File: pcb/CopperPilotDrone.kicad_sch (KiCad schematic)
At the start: 68 parts, among them IC1 TP4056, J1 USB_C_Receptacle_USB2.0, J2 Conn_01x02_Female, J3 B2B-PH-SM4-TB(LF)(SN), J4 Conn_01x02_Female, J5 Conn_01x02_Female, J6 Conn_01x02_Female, SW1 PCM12SMTR, SW2 TS-1187A, SW3 TS-1187A, T1 SI2302DS-T1, T2 SI2302DS-T1, T3 SI2302DS-T1, T4 SI2302DS-T1, U2 AO3401, U3 AP2112K-3.3TRG1, U8 ESP32-S3-WROOM-1-N8R8, U9 MPU-6050

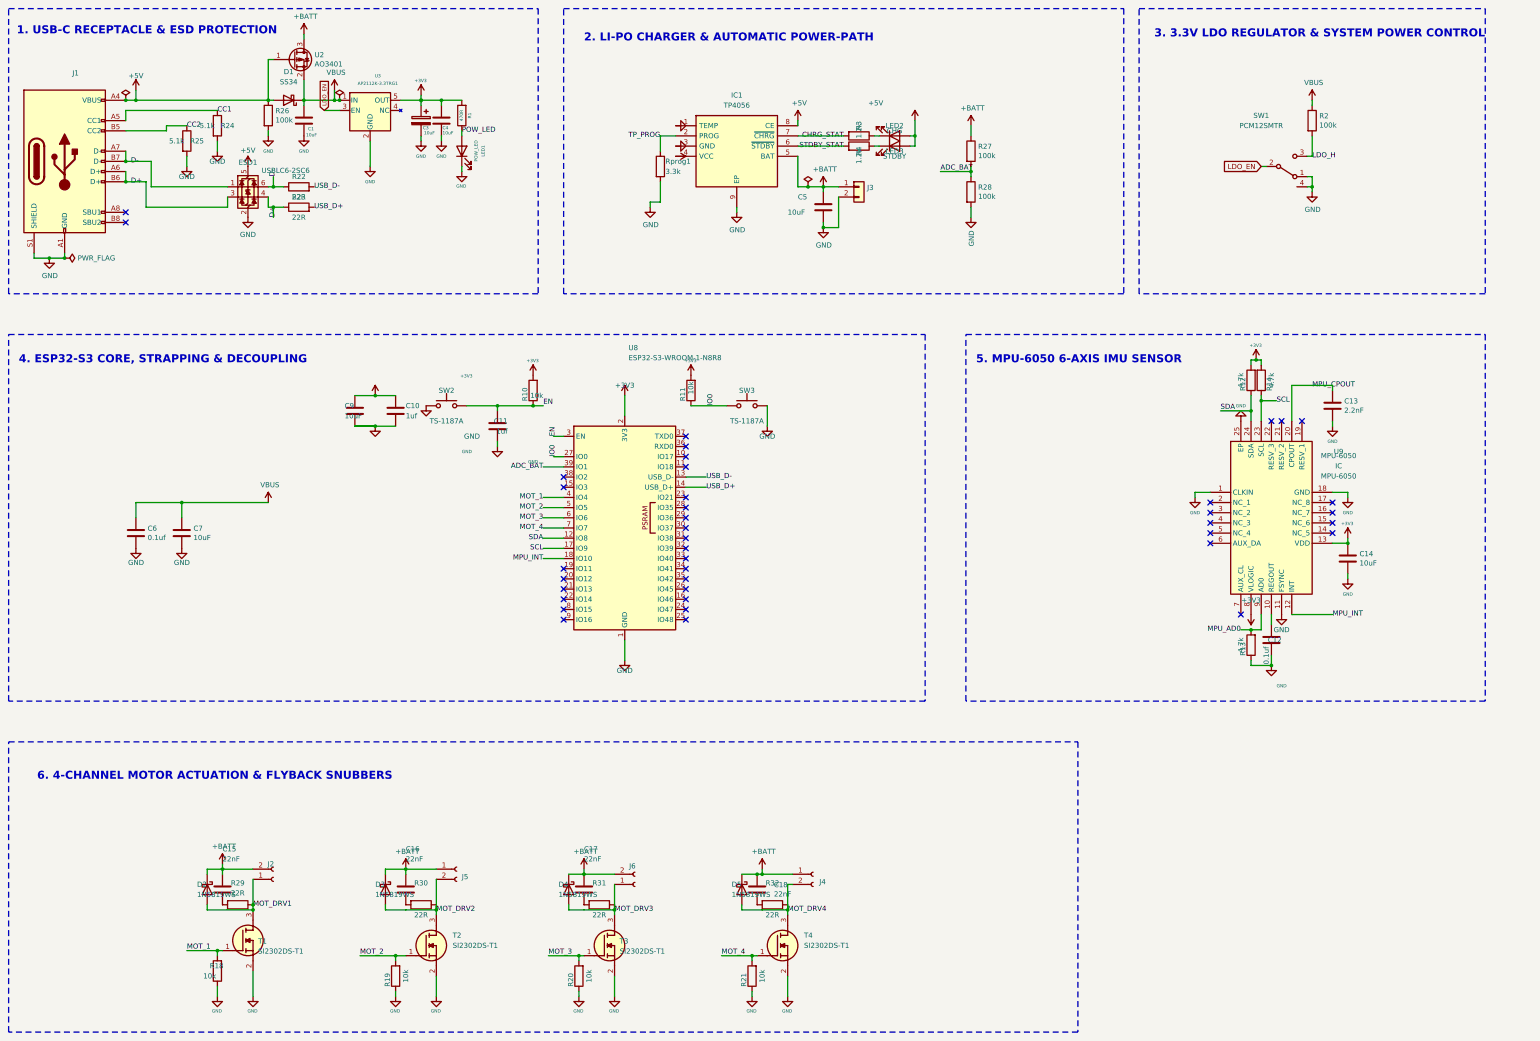
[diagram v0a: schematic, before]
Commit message: feat(pcb,sch,fw): migrate IC1 to MCP73833-AMI/UN and U9 to ICM-42670-P for 100% turnkey PCBA
Replace IC1 (TP4056 ESOP-8) with Microchip MCP73833-AMI/UN (MSOP-10) plus R15 10k THERM bias resistor and replace U9 (MPU-6050 QFN-24) with TDK ICM-42670-P (2.5x3.0mm LGA-14), achieving 0 ERC errors, 0 DRC violations, 0 unconnected items, and 100% turnkey LionCircuits BOM/CPL export with zero DNP.

Co-Authored-By: CopperPilot <noreply@copperpilot.ai>
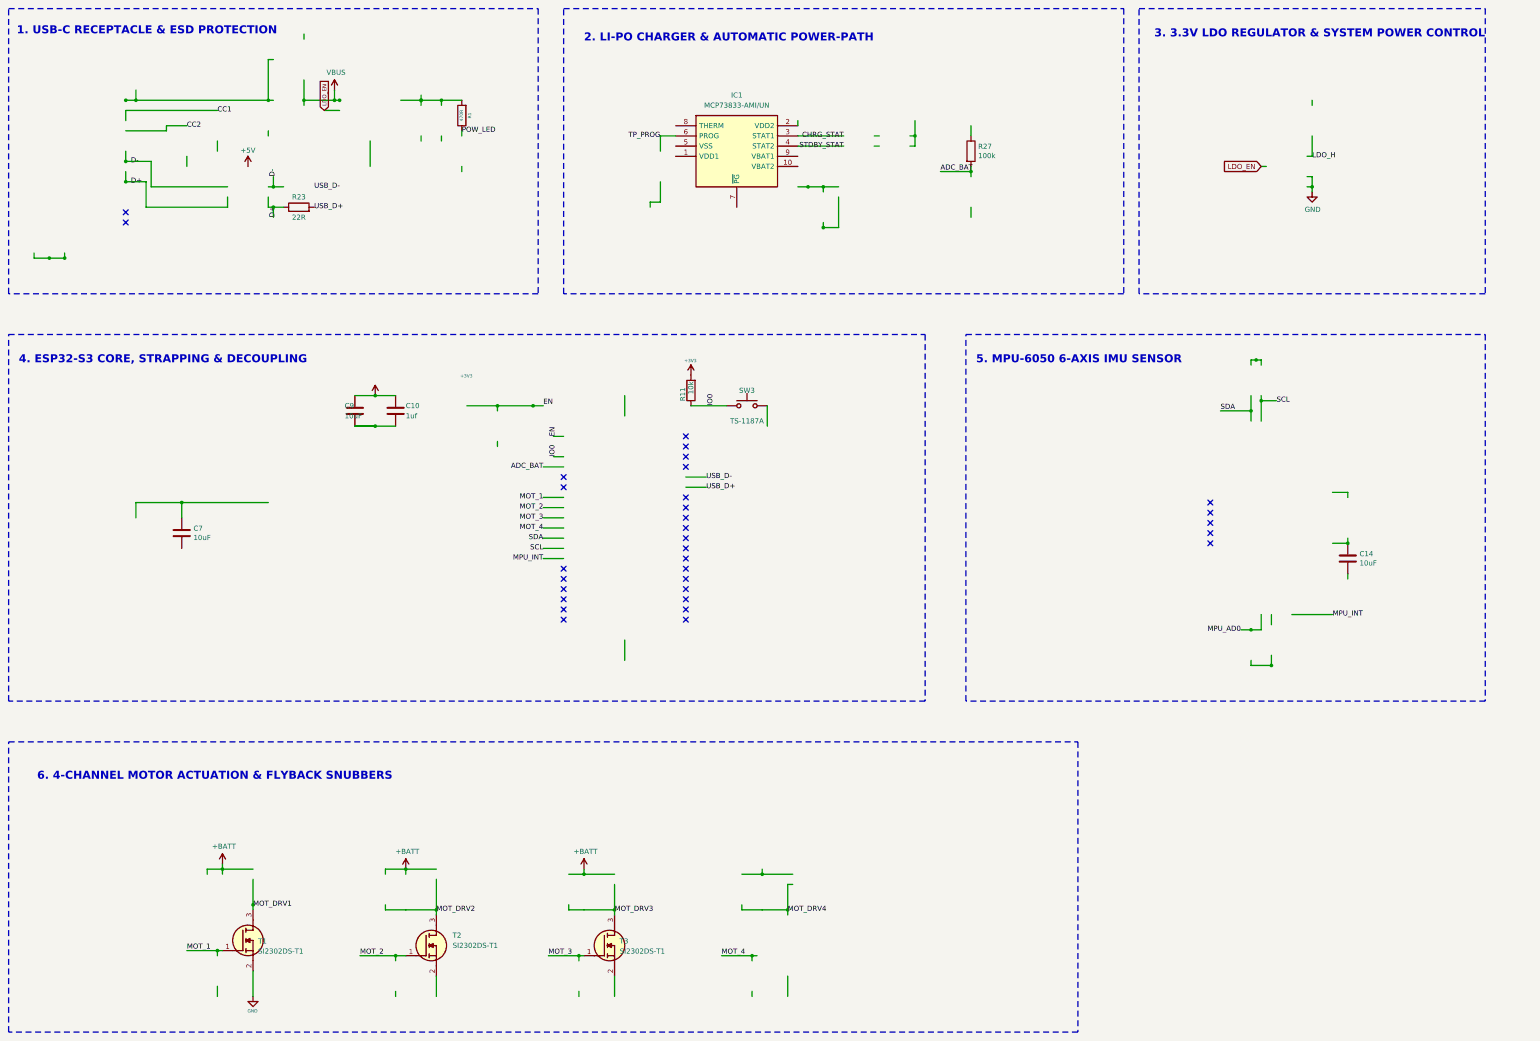
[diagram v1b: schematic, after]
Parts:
- removed C1, C4, C5: 10uF, Capacitor_SMD:C_0603_1608Metric, symbol Device:C
- removed C11: 1uf, Capacitor_SMD:C_0603_1608Metric, symbol Device:C
- removed C12, C6: 0.1uf, Capacitor_SMD:C_0603_1608Metric, symbol Device:C
- removed C13: 2.2nF, Capacitor_SMD:C_0603_1608Metric, symbol Device:C
- removed C15, C16, C17, C18: 22nF, Capacitor_SMD:C_0603_1608Metric, symbol Device:C
- removed C3: 10uF, Capacitor_SMD:C_0603_1608Metric, symbol Device:C_Polarized
- removed D1: SS34, Diode_SMD:D_SMA, symbol Diode:SS34
- removed D2, D3, D4, D5: 1N5819WS, Diode_SMD:D_SOD-323, symbol Diode:1N5819WS
- removed ESD1: USBLC6-2SC6, Package_TO_SOT_SMD:SOT-23-6, symbol Power_Protection:USBLC6-2SC6
- removed J1: USB_C_Receptacle_USB2.0, Connector_USB:USB_C_Receptacle_HRO_TYPE-C-31-M-12, symbol downloader-rescue:USB_C_Receptacle_USB2.0-Connector
- removed J2, J4, J5, J6: Conn_01x02_Female, Connector_JST:JST_GH_SM02B-GHS-TB_1x02-1MP_P1.25mm_Horizontal, symbol Connector:Conn_01x02_Socket
- removed J3: B2B-PH-SM4-TB(LF)(SN), easyeda2kicad:CONN-SMD_B2B-PH-SM4-TB-LF-SN, symbol Connector_Generic:Conn_01x02
- removed LED1: POW_LED, LED_SMD:LED_0603_1608Metric, symbol Device:LED
- removed LED2: CHG, LED_SMD:LED_0603_1608Metric, symbol Device:LED
- removed LED3: STDBY, LED_SMD:LED_0603_1608Metric, symbol Device:LED
- removed R10, R18, R19, R20, R21: 10k, Resistor_SMD:R_0603_1608Metric, symbol Device:R
- removed R12, R13, R14: 4.7k, Resistor_SMD:R_0603_1608Metric, symbol Device:R
- removed R2, R26, R28: 100k, Resistor_SMD:R_0603_1608Metric, symbol Device:R
- removed R22, R29, R30, R31, R32: 22R, Resistor_SMD:R_0603_1608Metric, symbol Device:R
- removed R24, R25: 5.1k, Resistor_SMD:R_0603_1608Metric, symbol Device:R
- removed R3, R4: 1.2k, Resistor_SMD:R_0603_1608Metric, symbol Device:R
- removed Rprog1: 3.3k, Resistor_SMD:R_0603_1608Metric, symbol Device:R
- removed SW1: PCM12SMTR, ESP32_TouchDown_lib:slide switch spdt, symbol ESP32_TouchDown_lib:slide switch spdt
- removed SW2: TS-1187A, Button_Switch_SMD:SW_Push_1P1T_XKB_TS-1187A, symbol Switch:SW_Push
- removed T4: SI2302DS-T1, SI2302DS-T1:SOT95P237X112-3N, symbol SI2302DS-T1:SI2302DS-T1
- removed U2: AO3401, Package_TO_SOT_SMD:SOT-23, symbol Transistor_FET:AO3401A
- removed U3: AP2112K-3.3TRG1, Package_TO_SOT_SMD:SOT-23-5, symbol Regulator_Linear:MIC5219-3.3YM5
- removed U8: ESP32-S3-WROOM-1-N8R8, RF_Module:ESP32-S3-WROOM-1, symbol RF_Module:ESP32-S3-WROOM-1
- removed U9: MPU-6050, MPU6050:MPU6050, symbol MPU-6050:MPU-6050
- IC1: value TP4056 -> MCP73833-AMI/UN; footprint tp4056:SOIC127P600X175-9N -> Package_SO:MSOP-10_3x3mm_P0.5mm; symbol TP4056-42-ESOP8:TP4056-42-ESOP8 -> TP4056-42-ESOP8:MCP73833-AMI-UN; LCSC C16581 -> C47182; Manufacturer_Name Nanjing Extension Microelectronics -> Microchip; Manufacturer_Part_Number TP4056-42-ESOP8 -> MCP73833-AMI/UN
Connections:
- net +3V3: no longer C14.1, R1.2
- net +5V: no longer IC1.4 (VCC), IC1.8 (CE)
- net +BATT: no longer IC1.5 (BAT), R27.1
- net CHRG_STAT: now also IC1.3 (STAT1); no longer IC1.7 (~{CHRG})
- net GND: no longer C10.2, C14.2, C7.2, C9.2, IC1.1 (TEMP), IC1.3 (GND), IC1.9 (EP), SW3.2, T2.2 (S), T3.2 (S)
- net STDBY_STAT: now also IC1.4 (STAT2); no longer IC1.6 (~{STDBY})
- net TP_PROG: now also IC1.6 (PROG); no longer IC1.2 (PROG)
- net VBUS: no longer C7.1
- new net: C10.2, C9.2
- no-connect marks 40 -> 32
